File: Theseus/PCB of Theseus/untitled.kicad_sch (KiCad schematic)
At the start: 30 parts, among them J5 Conn_01x06_Socket, J6 Conn_01x06_Socket, J7 Conn_01x06_Socket, J8 Conn_01x06_Socket, Q1 DMG1012UW-7, Q2 DMG1012UW-7, U5 MAX6675

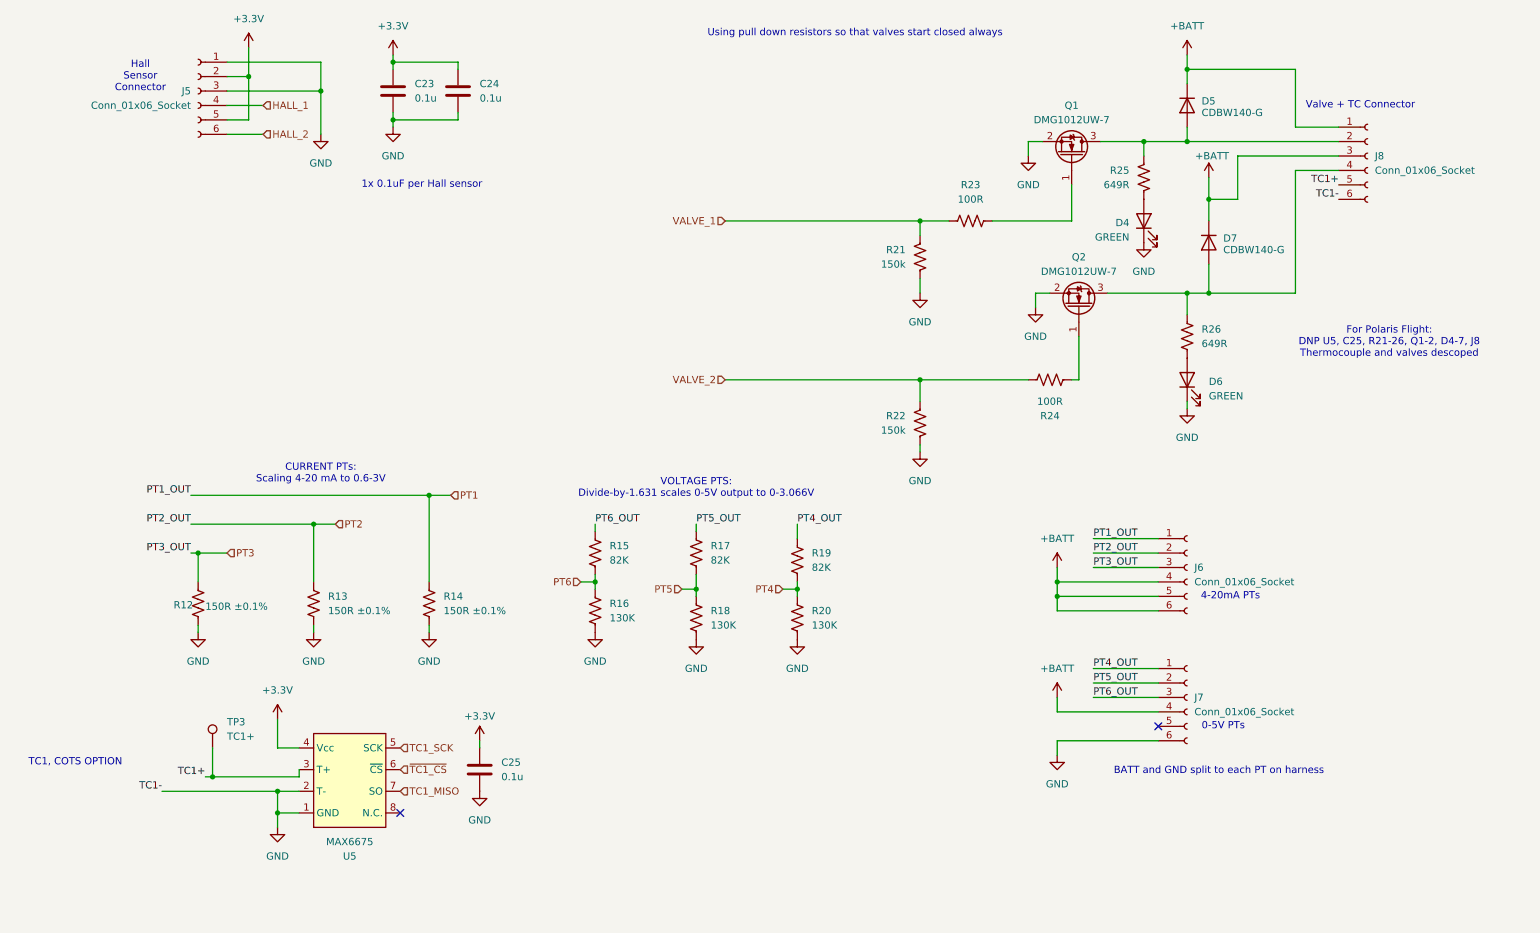
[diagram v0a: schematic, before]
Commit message: Changed the schematic to accommodate four 4-wire PTs
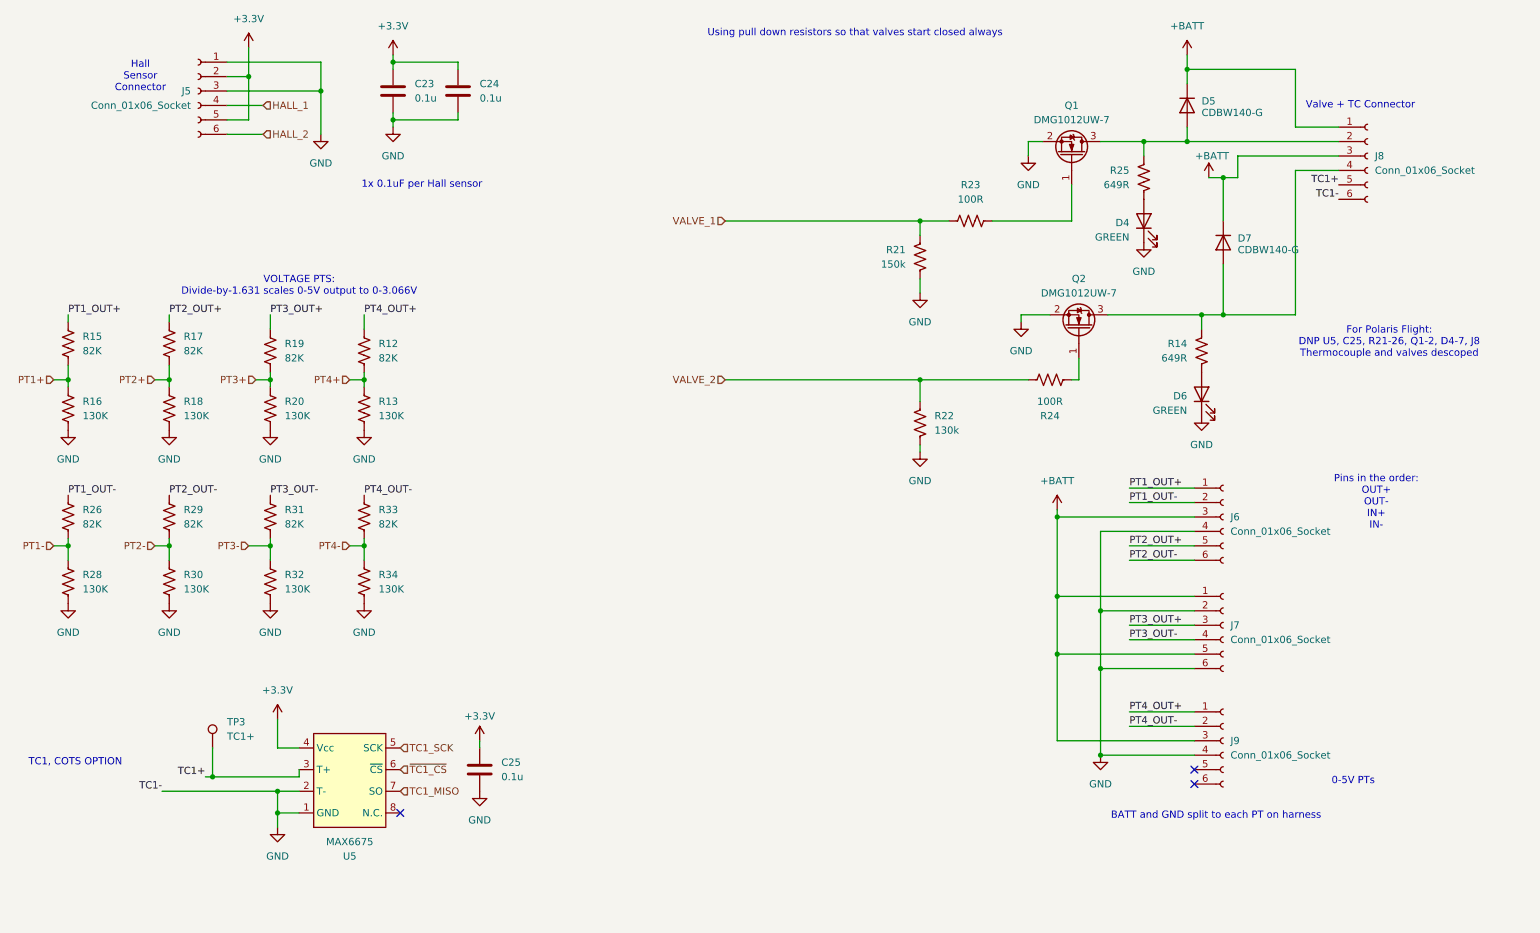
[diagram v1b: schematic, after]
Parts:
- added J9: Conn_01x06_Socket, symbol Connector:Conn_01x06_Socket
- added R28, R30, R32, R34: 130K, Resistor_SMD:R_0603_1608Metric_Pad0.98x0.95mm_HandSolder, symbol Device:R_US
- added R29, R31, R33: 82K, Resistor_SMD:R_0603_1608Metric_Pad0.98x0.95mm_HandSolder, symbol Device:R_US
- J6, J7: footprint canhw_footprints:connector_Harwin_G125–MG10605M4P -> (none)
- R12: value 150R ±0.1% -> 82K
- R13: value 150R ±0.1% -> 130K
- R14: value 150R ±0.1% -> 649R
- R22: value 150k -> 130k
- R26: value 649R -> 82K
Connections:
- net +BATT: now also J6.3 (Pin_3), J7.1 (Pin_1), J7.5 (Pin_5), J9.3 (Pin_3); no longer J6.4 (Pin_4), J6.5 (Pin_5), J6.6 (Pin_6), J7.4 (Pin_4)
- net GND: now also J6.4 (Pin_4), J7.2 (Pin_2), J9.4 (Pin_4), R28.2, R30.2, R32.2, R34.2; no longer R12.2, R14.2
- net at D7.2 (A), J8.4 (Pin_4), Q2.3 (D): now also R14.2; no longer R26.1
- net at D6.2 (A): now also R14.1; no longer R26.2
- net PT1 renamed PT1_OUT+
- net PT1_OUT+: now also R15.1; no longer R14.1
- net PT2 renamed PT1_OUT-
- net PT1_OUT-: now also R26.1; no longer R13.1
- net PT3 renamed PT4_OUT+
- net PT4_OUT+: now also J9.1 (Pin_1); no longer J6.3 (Pin_3)
- net PT4 renamed PT3+
- net PT4_OUT renamed PT3_OUT+
- net PT3_OUT+: now also J7.3 (Pin_3); no longer J7.1 (Pin_1)
- net PT5 renamed PT2+
- net PT5_OUT renamed PT2_OUT+
- net PT2_OUT+: now also J6.5 (Pin_5); no longer J7.2 (Pin_2)
- net PT6 renamed PT1+
- removed net PT6_OUT: J7.3 (Pin_3), R15.1
- new net PT1-: R26.2, R28.1
- new net PT2-: R29.2, R30.1
- new net PT2_OUT-: J6.6 (Pin_6), R29.1
- new net PT3-: R31.2, R32.1
- new net PT3_OUT-: J7.4 (Pin_4), R31.1
- new net PT4+: R12.2, R13.1
- new net PT4-: R33.2, R34.1
- new net PT4_OUT-: J9.2 (Pin_2), R33.1
- no-connect marks 2 -> 3
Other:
- note added: "Pins in the order: OUT+ OUT- IN+ IN-"
- note removed: "4-20mA PTs"
- note removed: "CURRENT PTs: Scaling 4-20 mA to 0.6-3V"
- moved on the sheet: R15, R16, R17, R18, R19, R20

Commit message: Swapped out the h7 STM to a H503RBT. Should have retained all pin functionality and tried to maintain physical pin positions so routing should be similar
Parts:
- J6, J7, J9: footprint (none) -> canhw_footprints:connector_Harwin_G125–MG10605M4P
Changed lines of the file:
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@@
 			)
 		)
-		(property "Footprint" ""
+		(property "Footprint" "canhw_footprints:connector_Harwin_G125–MG10605M4P"
 			(at 228.6 128.27 0)
 			(effects
@@
 			)
 		)
-		(property "Footprint" ""
+		(property "Footprint" "canhw_footprints:connector_Harwin_G125–MG10605M4P"
 			(at 228.6 109.22 0)
 			(effects
@@
 			)
 		)
-		(property "Footprint" ""
+		(property "Footprint" "canhw_footprints:connector_Harwin_G125–MG10605M4P"
 			(at 228.6 148.59 0)
 			(effects

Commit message: Added an entirely new file for the thermocouple in accordance with Jason H's design of a cheaper thermocouple circuit Also swapped out the STM H7 for a H5 with 64 pins. Everything should work fine but someone could confirm this if they have lots of free time
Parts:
- added TP4: TC1_TP, symbol Connector:TestPoint
- added TP5: TC2_TP, symbol Connector:TestPoint
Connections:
- new net TC_1: TP4.1
- new net TC_2: TP5.1
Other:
- added sheet Thermocouples (thermocouple stuff.kicad_sch)
- note added: "Still waiting on consensus on what connector we're using"
- note added: "TO BE DELETED ? I just didn't wanna delete it yet but yeah we're not using this"
- note added: "Test points added because the other TC had a test point so"
- note removed: "TC1, COTS OPTION"
- moved on the sheet: C25, TP3, U5
